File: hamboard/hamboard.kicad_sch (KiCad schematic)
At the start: 45 parts, among them J1 i2c, J10 Conn_01x03_Male, J2 Conn_01x24_Male, J3 USB_B_Micro, J4 Screw_Terminal_Btn, J5 Screw_Terminal_01x02, J6 programmer, Q1 AO3400A, Q2 S8050, Q3 S8050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

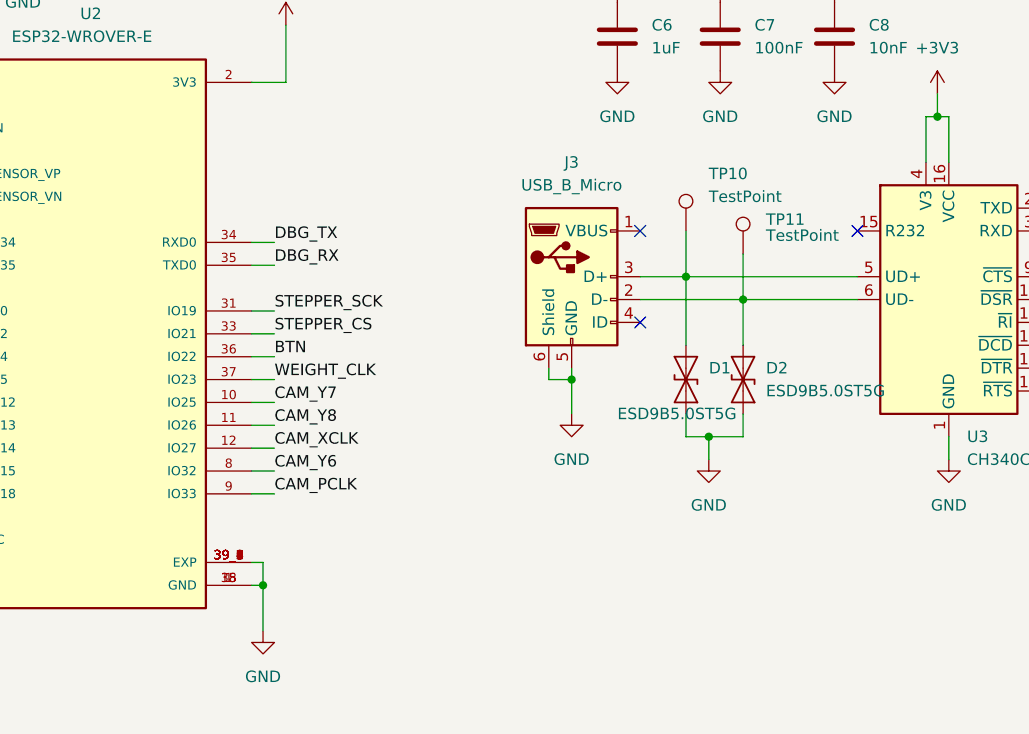
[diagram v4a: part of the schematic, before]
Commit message: board: fixed esp heat pads
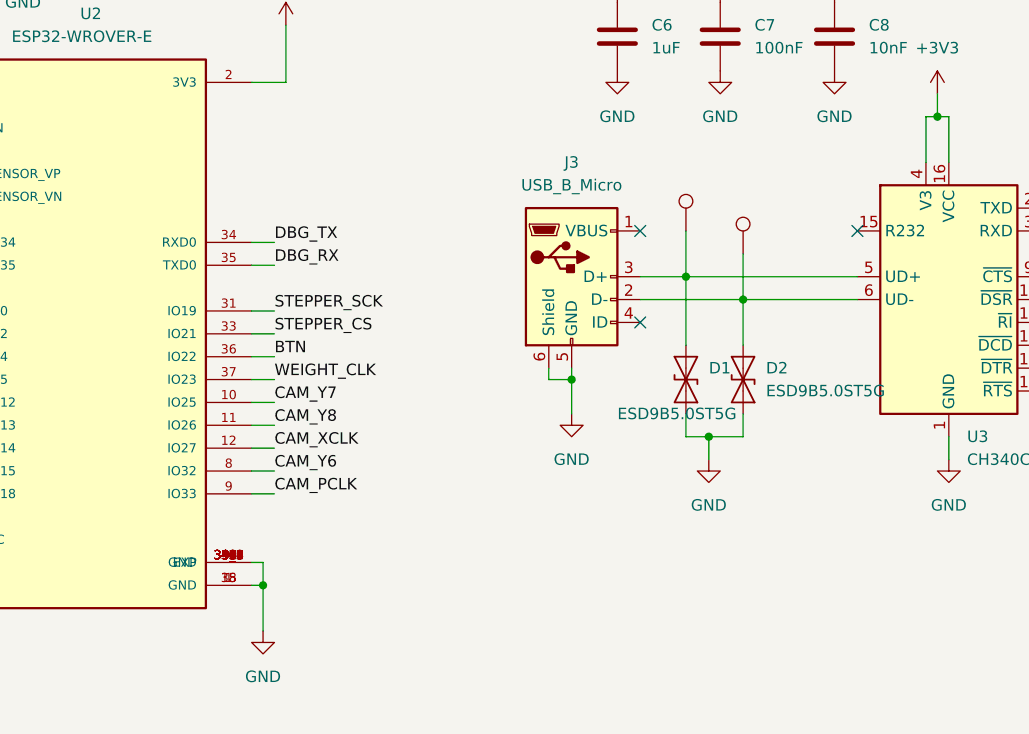
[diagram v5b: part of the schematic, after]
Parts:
- D1, D2: footprint hamboard:Diodes_DFN1006 -> Diode_SMD:D_SOD-923
- U3: footprint Package_SO:SOP-16_3.9x9.9mm_P1.27mm -> Package_SO:SOIC-16_3.9x9.9mm_P1.27mm
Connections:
- net GND: now also U2.40 (GND), U2.41 (GND), U2.42 (GND), U2.43 (GND), U2.44 (GND), U2.45 (GND), U2.46 (GND), U2.47 (GND), U2.48 (GND), U2.49 (GND), U2.50 (GND), U2.51 (GND)
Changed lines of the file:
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@@
       (effects (font (size 1.27 1.27)) hide)
     )
-    (property "Datasheet" "https://datasheet.lcsc.com/lcsc/2108150230_SHOU-HAN-0-5-24P-XGXJ-H2-0-119_C2858298.pdf" (id 3) (at 26.67 83.82 0)
+    (property "Datasheet" "~" (id 3) (at 26.67 83.82 0)
       (effects (font (size 1.27 1.27)) hide)
     )
@@
     (pin "39_9")
     (pin "4")
+    (pin "40")
+    (pin "41")
+    (pin "42")
+    (pin "43")
+    (pin "44")
+    (pin "45")
+    (pin "46")
+    (pin "47")
+    (pin "48")
+    (pin "49")
     (pin "5")
+    (pin "50")
+    (pin "51")
     (pin "6")
     (pin "7")
@@
       (effects (font (size 1.27 1.27)) hide)
     )
-    (property "Datasheet" "https://datasheet.lcsc.com/lcsc/2109011130_YONGYUTAI-S8050_C2891804.pdf" (id 3) (at 271.78 55.88 0)
+    (property "Datasheet" "~" (id 3) (at 271.78 55.88 0)
       (effects (font (size 1.27 1.27)) hide)
     )
@@
       (effects (font (size 1.27 1.27)) (justify right))
     )
-    (property "Footprint" "hamboard:Diodes_DFN1006" (id 2) (at 200.66 73.66 0)
+    (property "Footprint" "Diode_SMD:D_SOD-923" (id 2) (at 200.66 73.66 0)
       (effects (font (size 1.27 1.27)) hide)
     )
@@
       (effects (font (size 1.27 1.27)) (justify right))
     )
-    (property "Footprint" "hamboard:Diodes_DFN1006" (id 2) (at 194.31 73.66 0)
+    (property "Footprint" "Diode_SMD:D_SOD-923" (id 2) (at 194.31 73.66 0)
       (effects (font (size 1.27 1.27)) hide)
     )
@@
       (effects (font (size 1.27 1.27)) hide)
     )
-    (property "Datasheet" "https://datasheet.lcsc.com/lcsc/2109011130_YONGYUTAI-S8050_C2891804.pdf" (id 3) (at 271.78 80.01 0)
+    (property "Datasheet" "~" (id 3) (at 271.78 80.01 0)
       (effects (font (size 1.27 1.27)) hide)
     )
@@
       (effects (font (size 1.27 1.27)) (justify left))
     )
-    (property "Footprint" "Package_SO:SOP-16_3.9x9.9mm_P1.27mm" (id 2) (at 224.79 78.74 0)
+    (property "Footprint" "Package_SO:SOIC-16_3.9x9.9mm_P1.27mm" (id 2) (at 224.79 78.74 0)
       (effects (font (size 1.27 1.27)) (justify left) hide)
     )
@@
     (in_bom yes) (on_board yes)
     (property "Reference" "TP11" (id 0) (at 203.2 55.88 0)
-      (effects (font (size 1.27 1.27)) (justify left))
+      (effects (font (size 1.27 1.27)) (justify left) hide)
     )
     (property "Value" "TestPoint" (id 1) (at 203.2 57.6579 0)
-      (effects (font (size 1.27 1.27)) (justify left))
+      (effects (font (size 1.27 1.27)) (justify left) hide)
     )
     (property "Footprint" "TestPoint:TestPoint_Pad_D1.5mm" (id 2) (at 205.74 59.69 0)
@@
       (effects (font (size 1.27 1.27)) hide)
     )
-    (property "Datasheet" "https://datasheet.lcsc.com/lcsc/1811131827_Amphenol-ICC-10118193-0001LF_C132562.pdf" (id 3) (at 185.42 63.5 0)
+    (property "Datasheet" "~" (id 3) (at 185.42 63.5 0)
       (effects (font (size 1.27 1.27)) hide)
     )
@@
     (in_bom yes) (on_board yes)
     (property "Reference" "TP10" (id 0) (at 196.85 50.8 0)
-      (effects (font (size 1.27 1.27)) (justify left))
+      (effects (font (size 1.27 1.27)) (justify left) hide)
     )
     (property "Value" "TestPoint" (id 1) (at 196.85 53.34 0)
-      (effects (font (size 1.27 1.27)) (justify left))
+      (effects (font (size 1.27 1.27)) (justify left) hide)
     )
     (property "Footprint" "TestPoint:TestPoint_Pad_D1.5mm" (id 2) (at 199.39 57.15 0)
@@
     )
     (path "/4e27cb7d-b4a9-46e2-8603-b476a9c413d1"
-      (reference "D1") (unit 1) (value "ESD9B5.0ST5G") (footprint "hamboard:Diodes_DFN1006")
+      (reference "D1") (unit 1) (value "ESD9B5.0ST5G") (footprint "Diode_SMD:D_SOD-923")
     )
     (path "/47401035-5275-414e-9c65-ac7f7741871b"
-      (reference "D2") (unit 1) (value "ESD9B5.0ST5G") (footprint "hamboard:Diodes_DFN1006")
+      (reference "D2") (unit 1) (value "ESD9B5.0ST5G") (footprint "Diode_SMD:D_SOD-923")
     )
     (path "/cf781b29-da03-4e54-8f16-c9e2324f91c7/f98f2c3a-438b-43fd-8902-b43c6b39ee3b"
-      (reference "D3") (unit 1) (value "SD24_SOD523") (footprint "Diode_SMD:D_SOD-523")
+      (reference "D3") (unit 1) (value "SD24_SOD523") (footprint "Diode_SMD:D_SOD-323")
     )
     (path "/cf781b29-da03-4e54-8f16-c9e2324f91c7/9dec4aee-08f4-4a7b-bdfd-b6f95a08363b"
@@
     )
     (path "/5327a147-68fc-4492-abf9-1c498ebd9599/9612e1af-936e-46bb-b38f-d498561febb5"
-      (reference "TP4") (unit 1) (value "TestPoint") (footprint "TestPoint:TestPoint_Pad_D1.5mm")
+      (reference "TP4") (unit 1) (value "W_CLK") (footprint "TestPoint:TestPoint_Pad_D1.5mm")
     )
     (path "/cf781b29-da03-4e54-8f16-c9e2324f91c7/262ef5c4-4cf1-41b2-8ac5-4de463b38dbc"
-      (reference "TP7") (unit 1) (value "TestPoint") (footprint "TestPoint:TestPoint_Pad_D1.5mm")
+      (reference "TP7") (unit 1) (value "24V") (footprint "TestPoint:TestPoint_Pad_D1.5mm")
     )
     (path "/cf781b29-da03-4e54-8f16-c9e2324f91c7/ec254d83-55bb-4786-a17e-eae3949daeeb"
@@
     )
     (path "/907bf005-e0d6-4774-9e0e-39cb643d8799"
-      (reference "U3") (unit 1) (value "CH340C") (footprint "Package_SO:SOP-16_3.9x9.9mm_P1.27mm")
+      (reference "U3") (unit 1) (value "CH340C") (footprint "Package_SO:SOIC-16_3.9x9.9mm_P1.27mm")
     )
     (path "/5327a147-68fc-4492-abf9-1c498ebd9599/92af0034-9b27-4f45-a89a-63262bf31cd5"
